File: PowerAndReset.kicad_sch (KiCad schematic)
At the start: 21 parts, among them J4 USB4930-00-A_REVA, SW3 1825910-6, SW4 1825910-6, U2 AMS1117-3.3

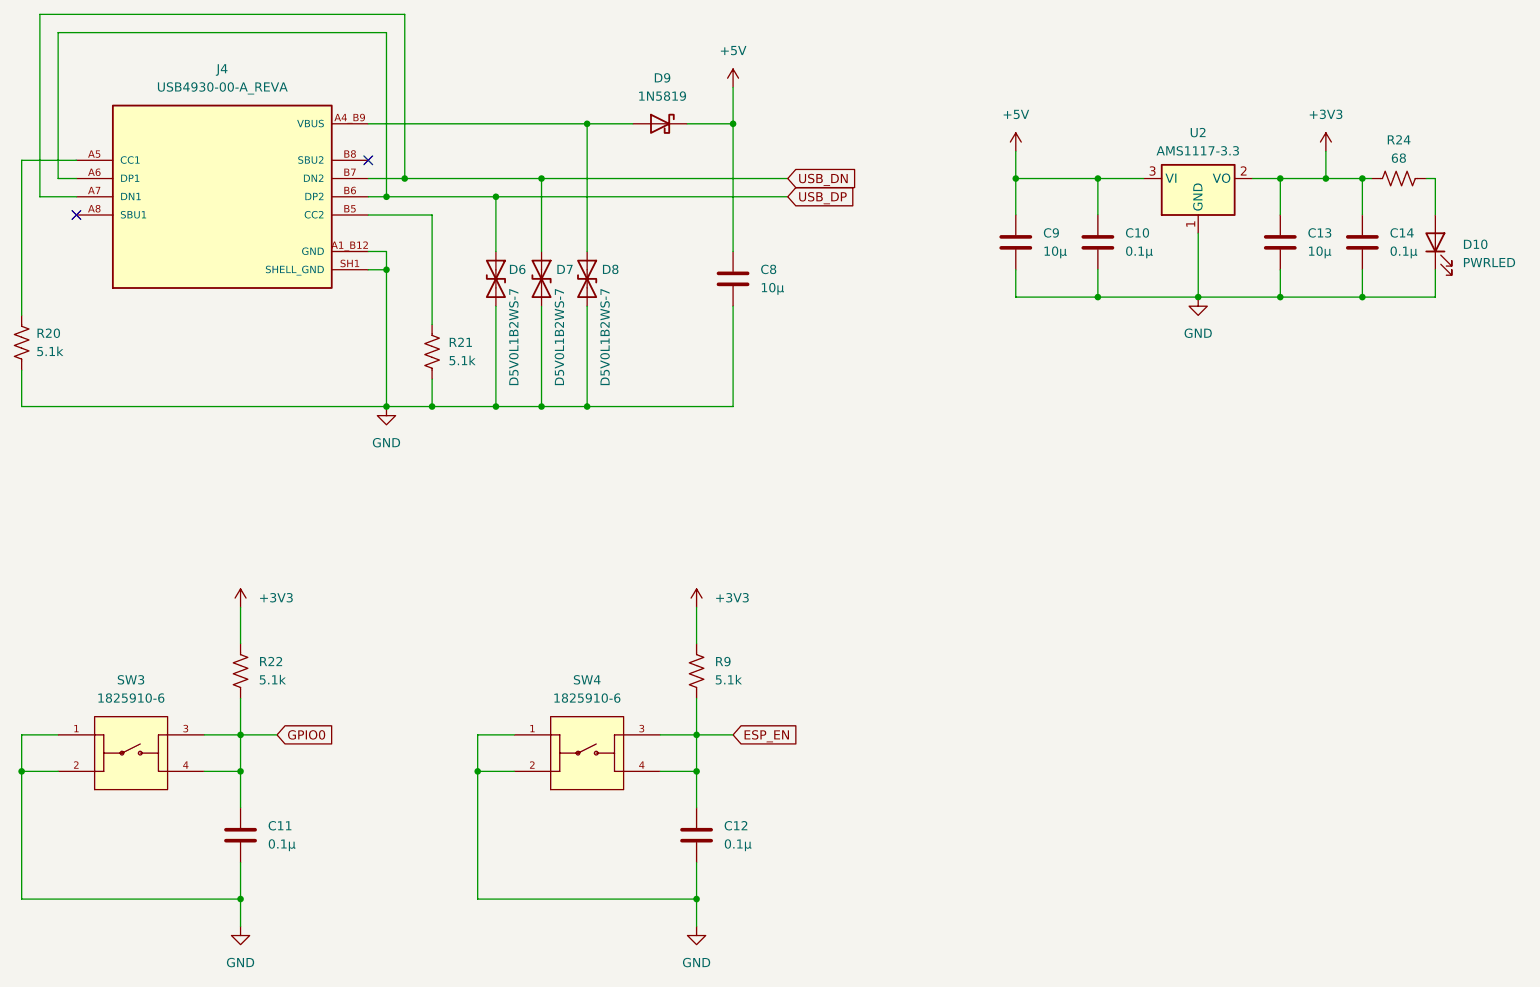
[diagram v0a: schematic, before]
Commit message: Adjust schematic 'no connect' symbols to prevent overlap
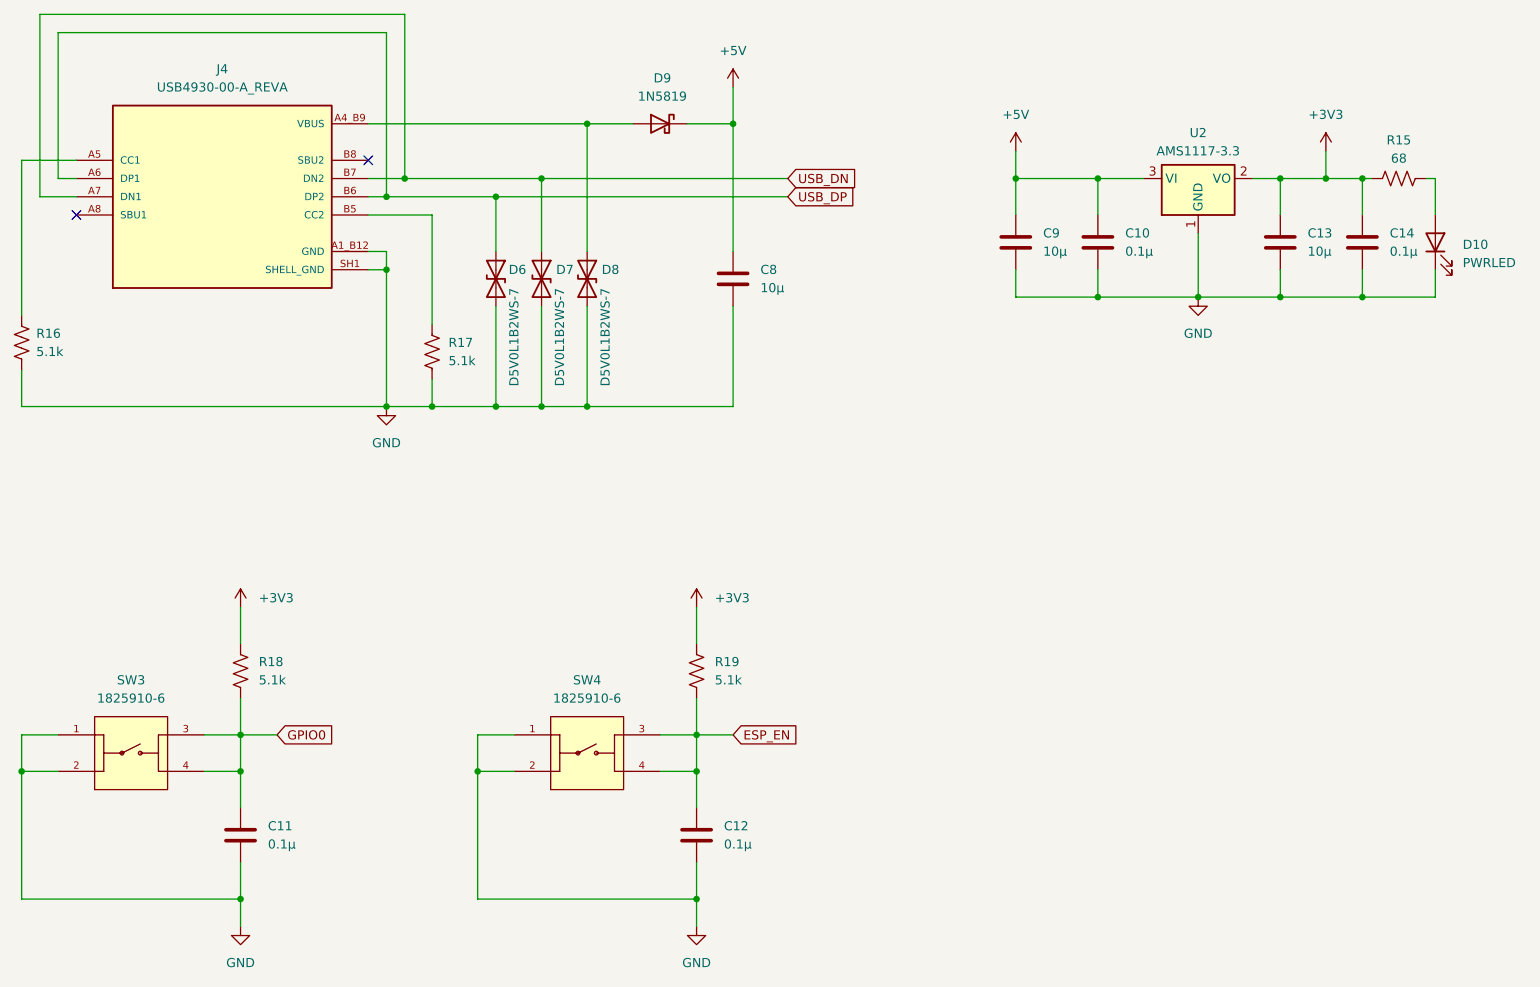
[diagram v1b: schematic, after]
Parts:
- renumbered R24 to R15, R20 to R16, R21 to R17, R22 to R18, R9 to R19
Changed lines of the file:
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@@
 		(on_board yes)
 		(dnp no)
-		(property "Reference" "R21"
+		(property "Reference" "R17"
 			(at 103.886 77.47 0)
 			(effects
@@
 			(project "AltWarriorsOfRock"
 				(path "/f99d3b67-4817-48a3-9376-1f8dc76dabe2/6e6e59bb-a0aa-487a-b8b3-5530ba753194"
-					(reference "R21")
+					(reference "R17")
 					(unit 1)
 				)
@@
 		(dnp no)
 		(fields_autoplaced yes)
-		(property "Reference" "R22"
+		(property "Reference" "R18"
 			(at 77.47 121.9199 0)
 			(effects
@@
 			(project "AltWarriorsOfRock"
 				(path "/f99d3b67-4817-48a3-9376-1f8dc76dabe2/6e6e59bb-a0aa-487a-b8b3-5530ba753194"
-					(reference "R22")
+					(reference "R18")
 					(unit 1)
 				)
@@
 		(on_board yes)
 		(dnp no)
-		(property "Reference" "R20"
+		(property "Reference" "R16"
 			(at 46.482 76.2 0)
 			(effects
@@
 			(project "AltWarriorsOfRock"
 				(path "/f99d3b67-4817-48a3-9376-1f8dc76dabe2/6e6e59bb-a0aa-487a-b8b3-5530ba753194"
-					(reference "R20")
+					(reference "R16")
 					(unit 1)
 				)
@@
 		(on_board yes)
 		(dnp no)
-		(property "Reference" "R24"
+		(property "Reference" "R15"
 			(at 236.22 49.276 90)
 			(effects
@@
 			(project "AltWarriorsOfRock"
 				(path "/f99d3b67-4817-48a3-9376-1f8dc76dabe2/6e6e59bb-a0aa-487a-b8b3-5530ba753194"
-					(reference "R24")
+					(reference "R15")
 					(unit 1)
 				)
@@
 		(dnp no)
 		(fields_autoplaced yes)
-		(property "Reference" "R9"
+		(property "Reference" "R19"
 			(at 140.97 121.9199 0)
 			(effects
@@
 			(project "AltWarriorsOfRock"
 				(path "/f99d3b67-4817-48a3-9376-1f8dc76dabe2/6e6e59bb-a0aa-487a-b8b3-5530ba753194"
-					(reference "R9")
-					(unit 1)
-				)
+					(reference "R19")
+					(unit 1)
+				)

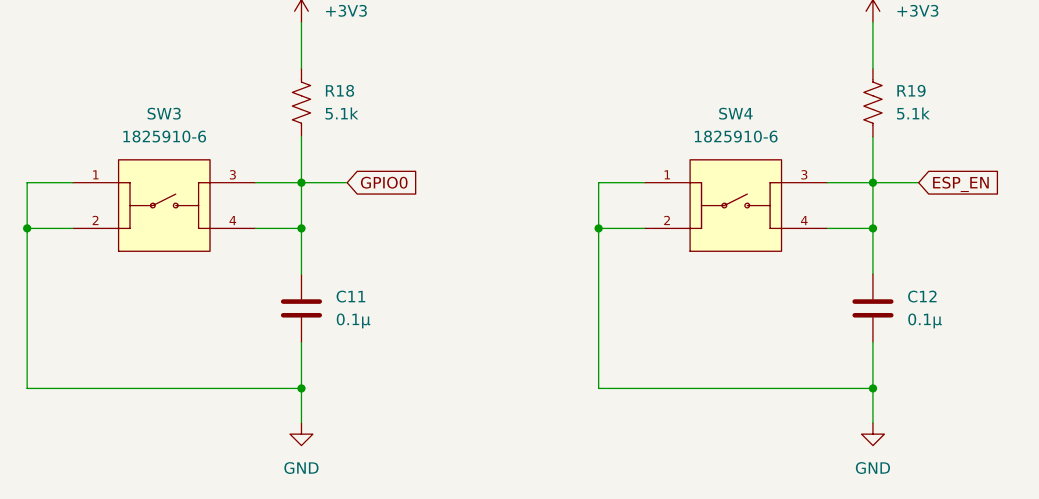
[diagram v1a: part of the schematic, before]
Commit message: Move C10, C14 closer to respective signals; thickened power/ground traces
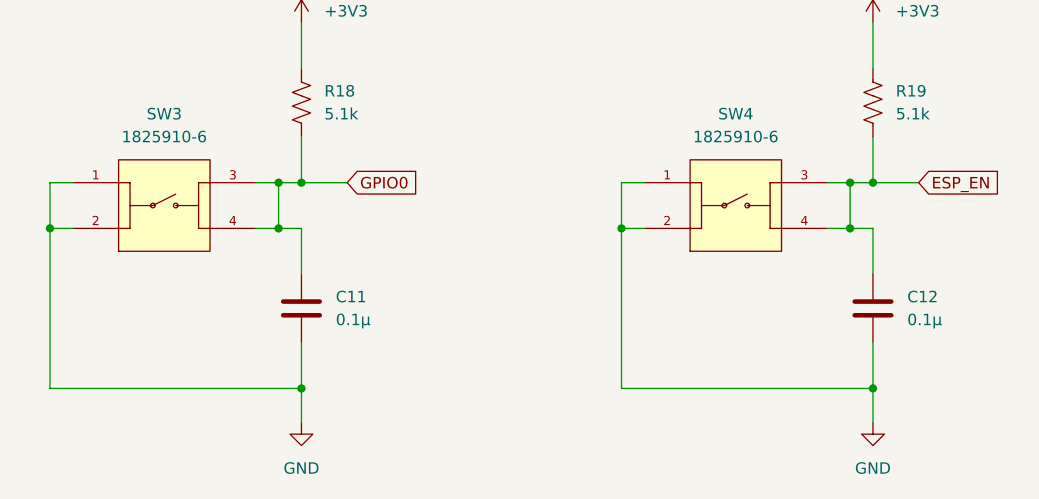
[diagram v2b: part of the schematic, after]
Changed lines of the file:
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@@
-	)
-	(junction
-		(at 107.95 137.16)
-		(diameter 0)
-		(color 0 0 0 0)
 	)
 	(junction
@@
 	)
 	(junction
+		(at 72.39 132.08)
+		(diameter 0)
+		(color 0 0 0 0)
+	)
+	(junction
 		(at 123.19 46.99)
 		(diameter 0)
@@
 	)
 	(junction
+		(at 135.89 132.08)
+		(diameter 0)
+		(color 0 0 0 0)
+	)
+	(junction
 		(at 74.93 132.08)
 		(diameter 0)
@@
 	)
 	(junction
-		(at 138.43 137.16)
-		(diameter 0)
-		(color 0 0 0 0)
-	)
-	(junction
 		(at 231.14 54.61)
 		(diameter 0)
@@
 	)
 	(junction
-		(at 44.45 137.16)
+		(at 46.99 137.16)
+		(diameter 0)
+		(color 0 0 0 0)
+	)
+	(junction
+		(at 135.89 137.16)
 		(diameter 0)
 		(color 0 0 0 0)
@@
 	)
 	(junction
+		(at 72.39 137.16)
+		(diameter 0)
+		(color 0 0 0 0)
+	)
+	(junction
 		(at 231.14 71.12)
 		(diameter 0)
@@
 	)
 	(junction
-		(at 74.93 137.16)
+		(at 110.49 137.16)
 		(diameter 0)
 		(color 0 0 0 0)
@@
 	(wire
 		(pts
-			(xy 69.85 132.08) (xy 74.93 132.08)
+			(xy 69.85 132.08) (xy 72.39 132.08)
 		)
 		(stroke
@@
 	(wire
 		(pts
-			(xy 107.95 132.08) (xy 107.95 137.16)
+			(xy 135.89 137.16) (xy 138.43 137.16)
+		)
+		(stroke
+			(width 0)
+			(type default)
+		)
+	)
+	(wire
+		(pts
+			(xy 110.49 132.08) (xy 110.49 137.16)
 		)
 		(stroke
@@
 	(wire
 		(pts
-			(xy 107.95 137.16) (xy 113.03 137.16)
-		)
-		(stroke
-			(width 0)
-			(type default)
-		)
-	)
-	(wire
-		(pts
 			(xy 138.43 154.94) (xy 138.43 158.75)
 		)
@@
 	(wire
 		(pts
-			(xy 44.45 137.16) (xy 49.53 137.16)
+			(xy 46.99 137.16) (xy 49.53 137.16)
 		)
 		(stroke
@@
 	(wire
 		(pts
-			(xy 138.43 132.08) (xy 138.43 137.16)
+			(xy 135.89 132.08) (xy 135.89 137.16)
 		)
 		(stroke
@@
 	(wire
 		(pts
-			(xy 113.03 132.08) (xy 107.95 132.08)
+			(xy 135.89 132.08) (xy 138.43 132.08)
+		)
+		(stroke
+			(width 0)
+			(type default)
+		)
+	)
+	(wire
+		(pts
+			(xy 113.03 132.08) (xy 110.49 132.08)
 		)
 		(stroke
@@
 	(wire
 		(pts
-			(xy 107.95 137.16) (xy 107.95 154.94)
+			(xy 110.49 137.16) (xy 110.49 154.94)
 		)
 		(stroke
@@
 	(wire
 		(pts
-			(xy 49.53 132.08) (xy 44.45 132.08)
+			(xy 49.53 132.08) (xy 46.99 132.08)
 		)
 		(stroke
@@
 	(wire
 		(pts
-			(xy 74.93 132.08) (xy 74.93 137.16)
+			(xy 72.39 132.08) (xy 72.39 137.16)
 		)
 		(stroke
@@
 	(wire
 		(pts
-			(xy 133.35 132.08) (xy 138.43 132.08)
+			(xy 133.35 132.08) (xy 135.89 132.08)
+		)
+		(stroke
+			(width 0)
+			(type default)
+		)
+	)
+	(wire
+		(pts
+			(xy 72.39 132.08) (xy 74.93 132.08)
 		)
 		(stroke
@@
 	(wire
 		(pts
-			(xy 44.45 132.08) (xy 44.45 137.16)
+			(xy 46.99 132.08) (xy 46.99 137.16)
 		)
 		(stroke
@@
 	(wire
 		(pts
-			(xy 69.85 137.16) (xy 74.93 137.16)
+			(xy 69.85 137.16) (xy 72.39 137.16)
 		)
 		(stroke
@@
 	(wire
 		(pts
-			(xy 44.45 137.16) (xy 44.45 154.94)
-		)
-		(stroke
-			(width 0)
-			(type default)
-		)
-	)
-	(wire
-		(pts
-			(xy 107.95 154.94) (xy 138.43 154.94)
+			(xy 46.99 137.16) (xy 46.99 154.94)
+		)
+		(stroke
+			(width 0)
+			(type default)
+		)
+	)
+	(wire
+		(pts
+			(xy 110.49 154.94) (xy 138.43 154.94)
 		)
 		(stroke
@@
 	(wire
 		(pts
-			(xy 44.45 154.94) (xy 74.93 154.94)
+			(xy 46.99 154.94) (xy 74.93 154.94)
 		)
 		(stroke
@@
 	(wire
 		(pts
+			(xy 72.39 137.16) (xy 74.93 137.16)
+		)
+		(stroke
+			(width 0)
+			(type default)
+		)
+	)
+	(wire
+		(pts
 			(xy 231.14 67.31) (xy 231.14 71.12)
 		)
@@
 	(wire
 		(pts
+			(xy 110.49 137.16) (xy 113.03 137.16)
+		)
+		(stroke
+			(width 0)
+			(type default)
+		)
+	)
+	(wire
+		(pts
 			(xy 116.84 72.39) (xy 116.84 86.36)
 		)
@@
 	(wire
 		(pts
-			(xy 133.35 137.16) (xy 138.43 137.16)
-		)
-		(stroke
+			(xy 133.35 137.16) (xy 135.89 137.16)
+		)
+		(stroke
